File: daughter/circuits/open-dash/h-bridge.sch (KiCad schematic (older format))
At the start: 10 parts, among them Q10 Q_NPN_BEC, Q11 Q_AO3401A, Q14 Q_AO3400A, Q17 Q_AO3401A, Q20 Q_AO3400A, Q9 Q_NPN_BEC

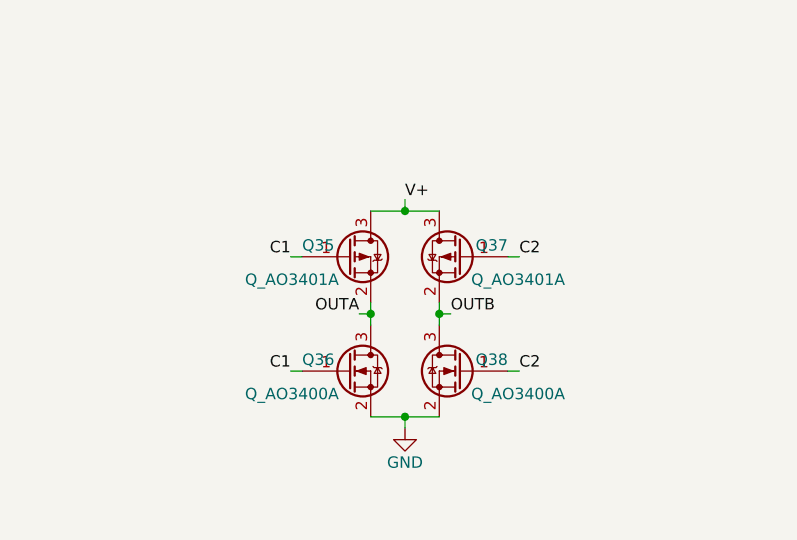
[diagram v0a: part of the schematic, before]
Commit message: send v1.4 to board house. Corrected source-drain on fets.
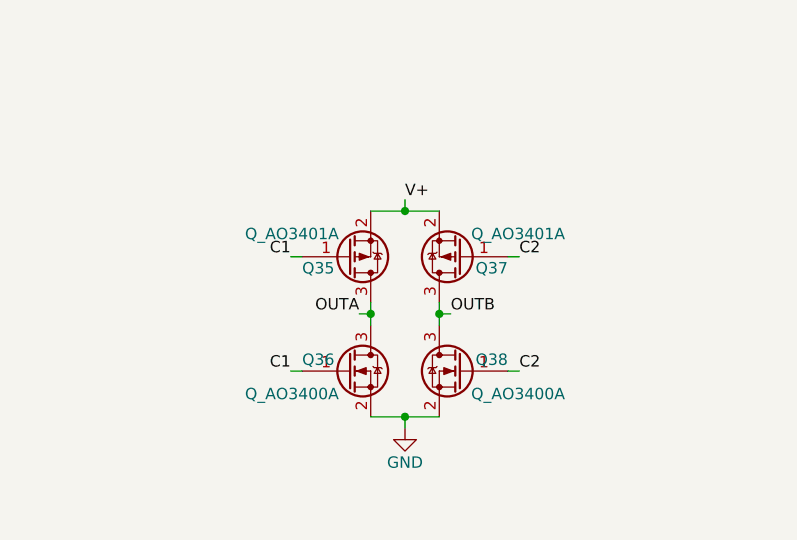
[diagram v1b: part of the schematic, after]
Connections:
- net OUTA: now also Q11.3 (D); no longer Q11.2 (S)
- net OUTB: now also Q17.3 (D); no longer Q17.2 (S)
- net V+: now also Q11.2 (S), Q17.2 (S); no longer Q11.3 (D), Q17.3 (D)
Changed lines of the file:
@@
 $Descr A4 11693 8268
 encoding utf-8
-Sheet 9 14
+Sheet 13 14
 Title ""
 Date ""
@@
 F 5 "C15127" H 5700 2200 50  0001 C CNN "LCSC"
 	1    5400 1950
-	1    0    0    -1
+	1    0    0    1
 $EndComp
 $Comp
@@
 F 5 "C15127" H 6200 2200 50  0001 C CNN "LCSC"
 	1    5900 1950
-	-1   0    0    -1
-$EndComp
-$Comp
+	-1   0    0    1
+$EndComp
+$Comp

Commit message: updated schematic
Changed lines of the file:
@@
 $Descr A4 11693 8268
 encoding utf-8
-Sheet 13 14
+Sheet 11 14
 Title ""
 Date ""
@@
 AR Path="/601F213A/60537FF7/6055EDDA" Ref="Q19"  Part="1"
 AR Path="/601F213A/607B7BA9/6055EDDA" Ref="Q22"  Part="1"
-F 0 "Q22" H 6791 4546 50  0000 L CNN
+F 0 "Q16" H 6791 4546 50  0000 L CNN
 F 1 "Q_NPN_BEC" H 6791 4455 50  0000 L CNN
 F 2 "Package_TO_SOT_SMD:SOT-23" H 6800 4600 50  0001 C CNN
@@
 AR Path="/601F213A/60537FF7/605659CE" Ref="R79"  Part="1"
 AR Path="/601F213A/607B7BA9/605659CE" Ref="R83"  Part="1"
-F 0 "R83" H 6770 4046 50  0000 L CNN
+F 0 "R75" H 6770 4046 50  0000 L CNN
 F 1 "R_10K_0402" H 6770 3955 50  0000 L CNN
 F 2 "Resistor_SMD:R_0402_1005Metric_Pad0.72x0.64mm_HandSolder" V 6630 4000 50  0001 C CNN
@@
 AR Path="/601F213A/60537FF7/6056BCEC" Ref="R78"  Part="1"
 AR Path="/601F213A/607B7BA9/6056BCEC" Ref="R82"  Part="1"
-F 0 "R82" V 5943 4500 50  0000 C CNN
+F 0 "R74" V 5943 4500 50  0000 C CNN
 F 1 "R_10K_0402" V 6034 4500 50  0000 C CNN
 F 2 "Resistor_SMD:R_0402_1005Metric_Pad0.72x0.64mm_HandSolder" V 6080 4500 50  0001 C CNN
@@
 AR Path="/601F213A/60537FF7/605EA495" Ref="#PWR0115"  Part="1"
 AR Path="/601F213A/607B7BA9/605EA495" Ref="#PWR0118"  Part="1"
-F 0 "#PWR0118" H 6700 4500 50  0001 C CNN
+F 0 "#PWR0112" H 6700 4500 50  0001 C CNN
 F 1 "GND" H 6700 4600 50  0000 C CNN
 F 2 "" H 6700 4750 50  0000 C CNN
@@
 AR Path="/601F213A/60537FF7/6062E0E9" Ref="Q18"  Part="1"
 AR Path="/601F213A/607B7BA9/6062E0E9" Ref="Q21"  Part="1"
-F 0 "Q21" H 5291 4546 50  0000 L CNN
+F 0 "Q15" H 5291 4546 50  0000 L CNN
 F 1 "Q_NPN_BEC" H 5291 4455 50  0000 L CNN
 F 2 "Package_TO_SOT_SMD:SOT-23" H 5300 4600 50  0001 C CNN
@@
 AR Path="/601F213A/60537FF7/6062E29F" Ref="R77"  Part="1"
 AR Path="/601F213A/607B7BA9/6062E29F" Ref="R81"  Part="1"
-F 0 "R81" H 5270 4046 50  0000 L CNN
+F 0 "R73" H 5270 4046 50  0000 L CNN
 F 1 "R_10K_0402" H 5270 3955 50  0000 L CNN
 F 2 "Resistor_SMD:R_0402_1005Metric_Pad0.72x0.64mm_HandSolder" V 5130 4000 50  0001 C CNN
@@
 AR Path="/601F213A/60537FF7/6062E2AB" Ref="R76"  Part="1"
 AR Path="/601F213A/607B7BA9/6062E2AB" Ref="R80"  Part="1"
-F 0 "R80" V 4443 4500 50  0000 C CNN
+F 0 "R72" V 4443 4500 50  0000 C CNN
 F 1 "R_10K_0402" V 4534 4500 50  0000 C CNN
 F 2 "Resistor_SMD:R_0402_1005Metric_Pad0.72x0.64mm_HandSolder" V 4580 4500 50  0001 C CNN
@@
 AR Path="/601F213A/60537FF7/6062E2B6" Ref="#PWR0114"  Part="1"
 AR Path="/601F213A/607B7BA9/6062E2B6" Ref="#PWR0117"  Part="1"
-F 0 "#PWR0117" H 5200 4500 50  0001 C CNN
+F 0 "#PWR0111" H 5200 4500 50  0001 C CNN
 F 1 "GND" H 5200 4600 50  0000 C CNN
 F 2 "" H 5200 4750 50  0000 C CNN
@@
 AR Path="/601F213A/60537FF7/619BDA1A" Ref="Q31"  Part="1"
 AR Path="/601F213A/607B7BA9/619BDA1A" Ref="Q35"  Part="1"
-F 0 "Q35" H 5200 2000 50  0000 L CNN
+F 0 "Q27" H 5200 2000 50  0000 L CNN
 F 1 "Q_AO3401A" H 4950 1850 50  0000 L CNN
 F 2 "Package_TO_SOT_SMD:SOT-23" H 5600 2050 50  0001 C CNN
@@
 AR Path="/601F213A/60537FF7/619CB5F7" Ref="Q32"  Part="1"
 AR Path="/601F213A/607B7BA9/619CB5F7" Ref="Q36"  Part="1"
-F 0 "Q36" H 5200 2500 50  0000 L CNN
+F 0 "Q28" H 5200 2500 50  0000 L CNN
 F 1 "Q_AO3400A" H 4950 2350 50  0000 L CNN
 F 2 "Package_TO_SOT_SMD:SOT-23" H 5600 2550 50  0001 C CNN
@@
 AR Path="/601F213A/60537FF7/619F76B8" Ref="Q33"  Part="1"
 AR Path="/601F213A/607B7BA9/619F76B8" Ref="Q37"  Part="1"
-F 0 "Q37" H 5700 2000 50  0000 L CNN
+F 0 "Q29" H 5700 2000 50  0000 L CNN
 F 1 "Q_AO3401A" H 5450 1850 50  0000 L CNN
 F 2 "Package_TO_SOT_SMD:SOT-23" H 6100 2050 50  0001 C CNN
@@
 AR Path="/601F213A/60537FF7/619F7C84" Ref="Q34"  Part="1"
 AR Path="/601F213A/607B7BA9/619F7C84" Ref="Q38"  Part="1"
-F 0 "Q38" H 5700 2500 50  0000 L CNN
+F 0 "Q30" H 5700 2500 50  0000 L CNN
 F 1 "Q_AO3400A" H 5450 2350 50  0000 L CNN
 F 2 "Package_TO_SOT_SMD:SOT-23" H 6100 2550 50  0001 C CNN
@@
 AR Path="/601F213A/60537FF7/61A2F624" Ref="#PWR0161"  Part="1"
 AR Path="/601F213A/607B7BA9/61A2F624" Ref="#PWR0174"  Part="1"
-F 0 "#PWR0174" H 5650 2450 50  0001 C CNN
+F 0 "#PWR0160" H 5650 2450 50  0001 C CNN
 F 1 "GND" H 5650 2550 50  0000 C CNN
 F 2 "" H 5650 2700 50  0000 C CNN
